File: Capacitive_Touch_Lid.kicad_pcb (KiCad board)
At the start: 2 copper layers, 65 x 31.4 mm, 14 parts, among them J1 Conn_02x20_Odd_Even

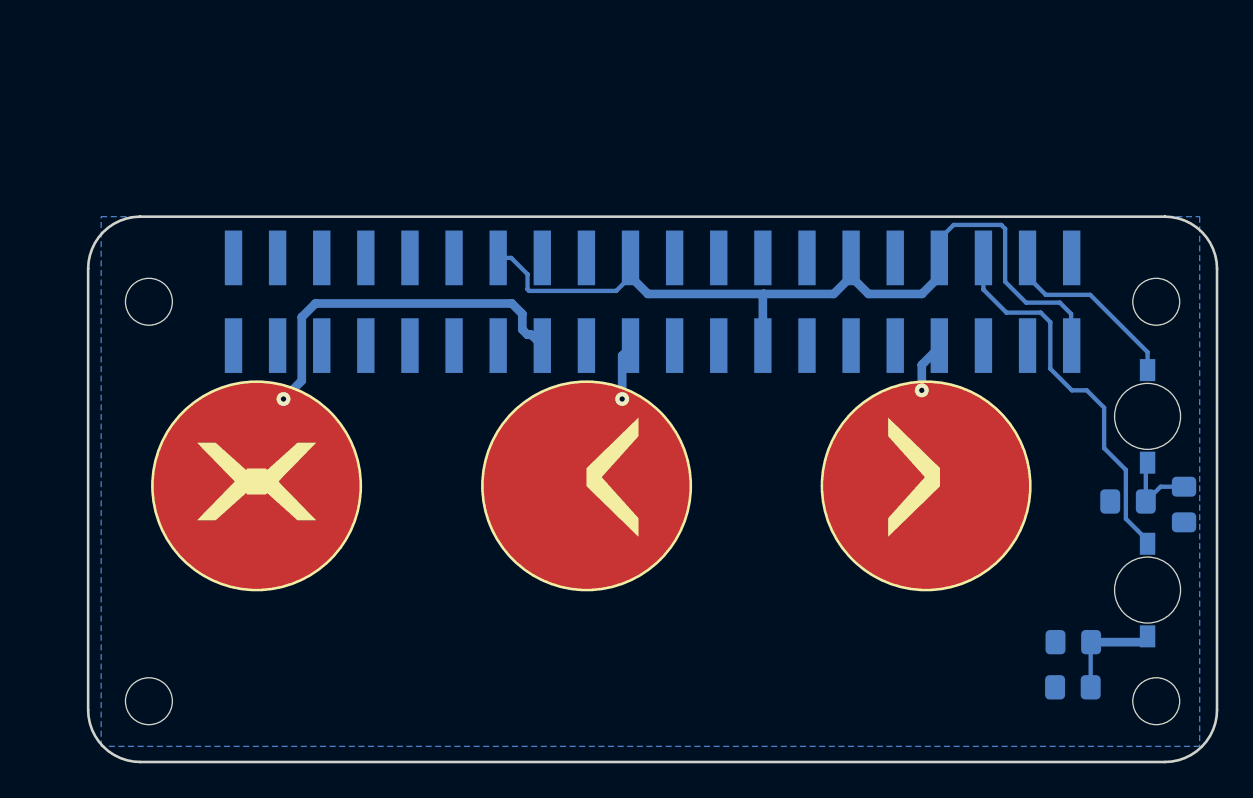
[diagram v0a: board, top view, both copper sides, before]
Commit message: Flipped board
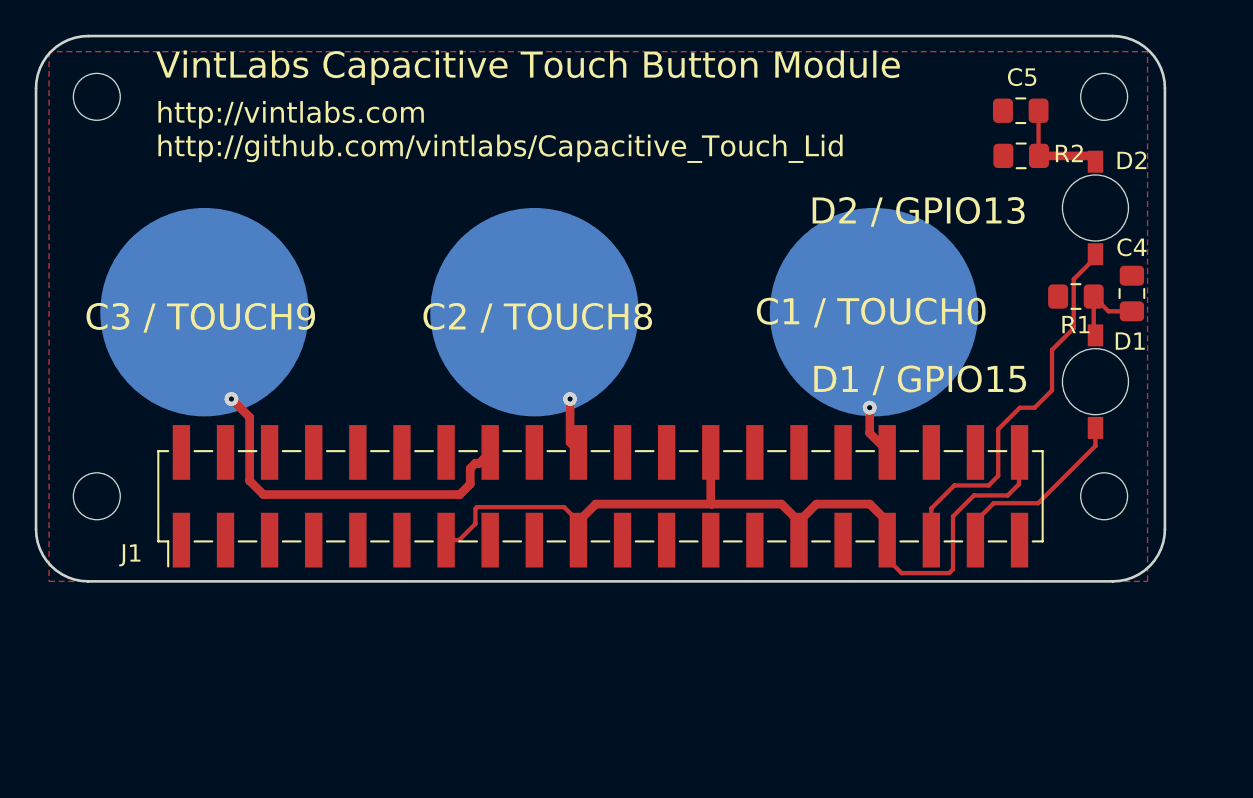
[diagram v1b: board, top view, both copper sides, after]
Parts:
- C1, C2, C3, REF** (x4): moved to B.Cu
- C4, C5, D1, D2, J1, R1, R2: moved to F.Cu
- moved REF** 34.9 mm to (86.0, 81.6)
- moved REF** 34.9 mm to (144.0, 81.6)
- moved C5 33.3 mm to (139.2, 82.4)
- moved R2 28.2 mm to (139.2, 85.0)
- moved D2 22.2 mm to (143.5, 88.0), turned to 270 degrees
- moved C4 12.5 mm to (145.6, 92.9), turned to 90 degrees
- moved R1 12.2 mm to (142.4, 93.1)
- moved J1 11.6 mm to (115.0, 104.6), turned to 90 degrees
- moved REF** 11.6 mm to (144.0, 104.6)
- moved REF** 11.6 mm to (86.0, 104.6)
- moved C1 10.4 mm to (130.8, 94.0)
- moved C2 10.4 mm to (111.2, 94.0)
- moved C3 10.4 mm to (92.2, 94.0)
- moved D1 3.61 mm to (143.5, 98.0), turned to 270 degrees
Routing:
- added copper zone on F.Cu, net GND
- removed copper zone on B.Cu, net GND
